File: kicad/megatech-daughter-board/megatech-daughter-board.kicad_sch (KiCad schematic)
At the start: 2 parts, among them J1 Conn_02x20_Counter_Clockwise, U1 Z084000xP

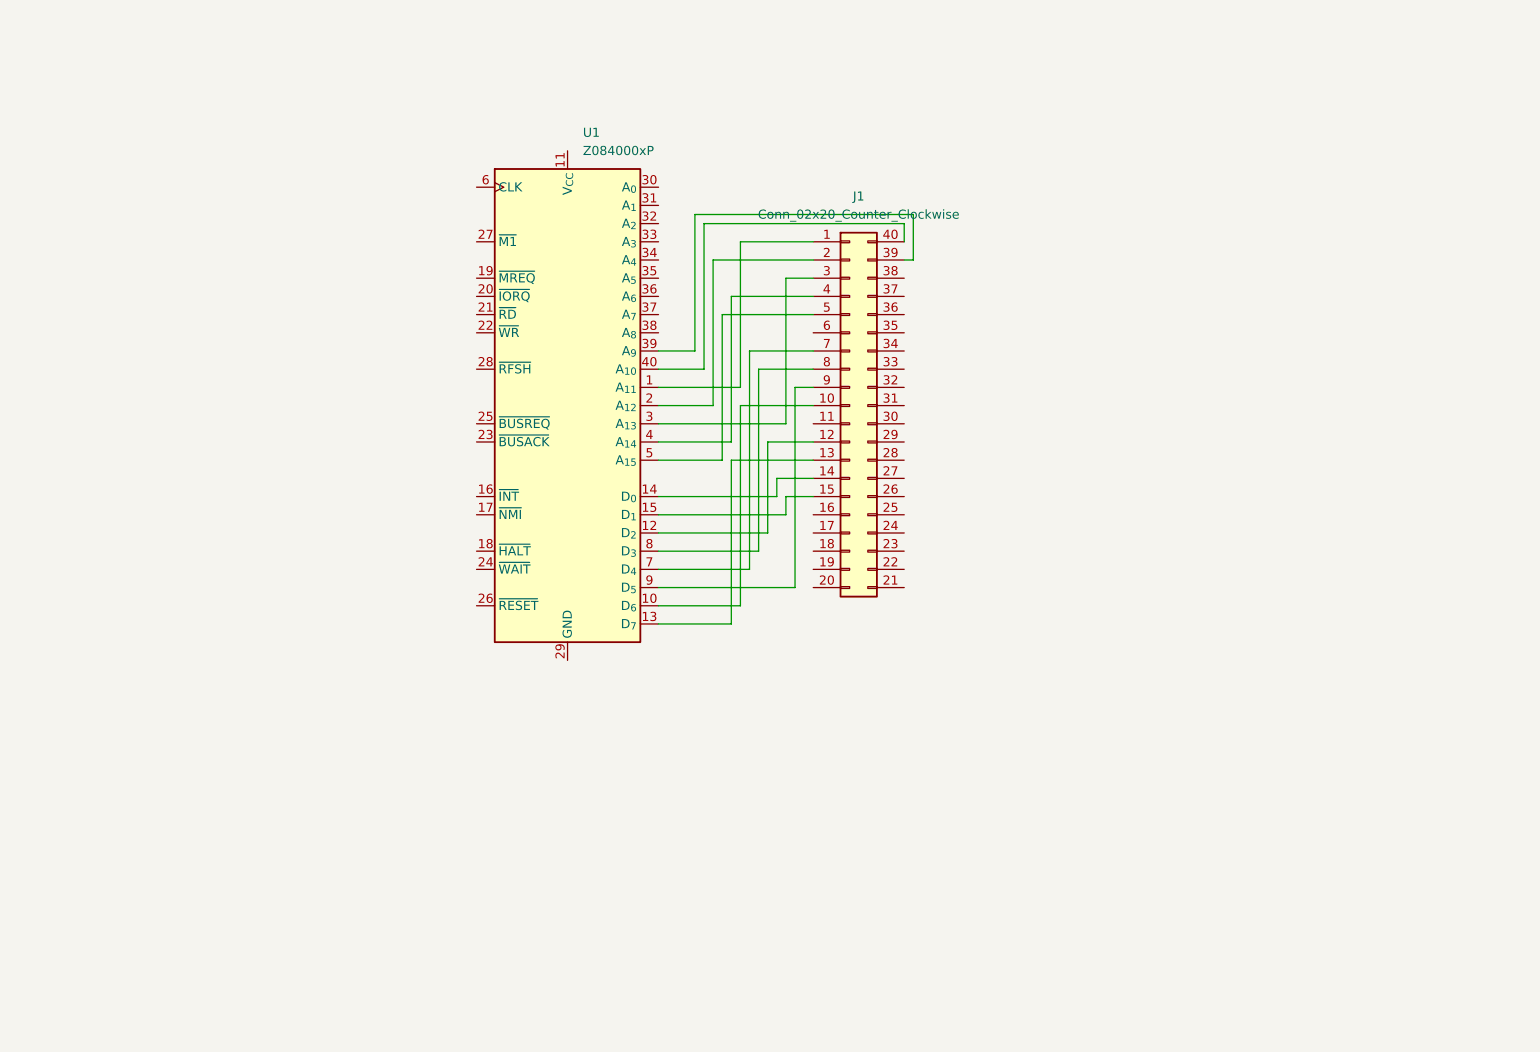
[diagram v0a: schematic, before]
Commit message: Placing more symbols
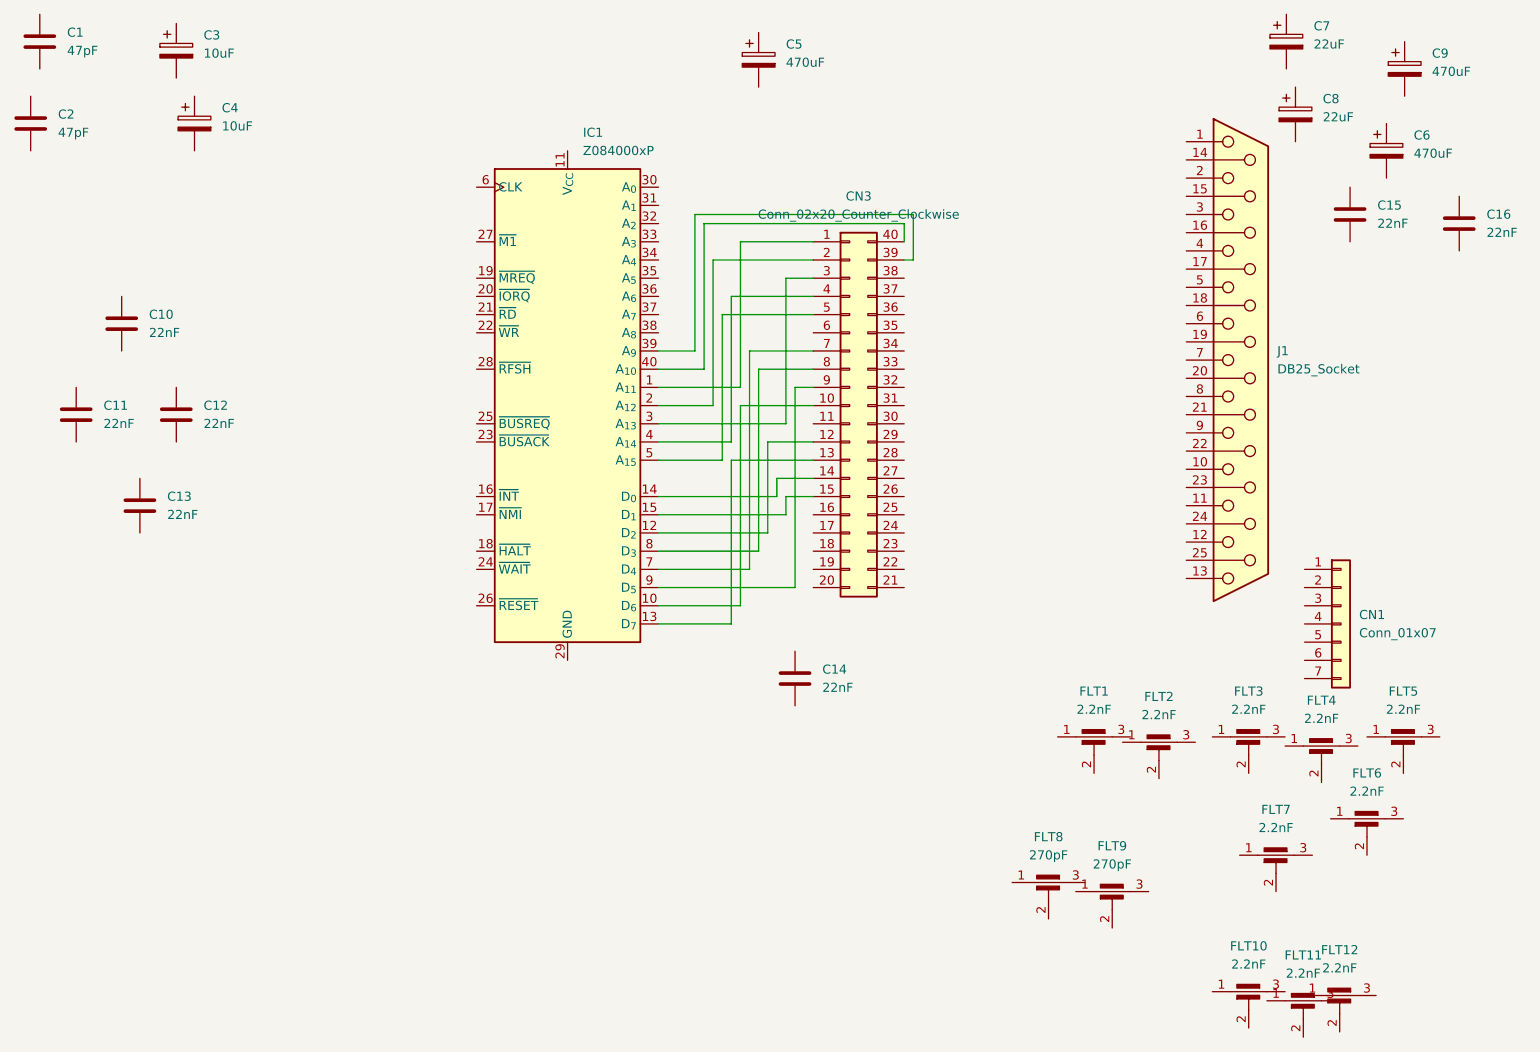
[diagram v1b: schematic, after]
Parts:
- added C1, C2: 47pF, Capacitor_THT:C_Disc_D4.3mm_W1.9mm_P5.00mm, symbol Device:C
- added C10, C11, C12, C13, C14, C15, C16: 22nF, Capacitor_THT:C_Disc_D6.0mm_W2.5mm_P5.00mm, symbol Device:C
- added C3, C4: 10uF, Capacitor_THT:C_Radial_D8.0mm_H11.5mm_P3.50mm, symbol Device:C_Polarized
- added C5, C6, C9: 470uF, Capacitor_THT:C_Radial_D10.0mm_H16.0mm_P5.00mm, symbol Device:C_Polarized
- added C7, C8: 22uF, Capacitor_THT:C_Radial_D8.0mm_H11.5mm_P3.50mm, symbol Device:C_Polarized
- added CN1: Conn_01x07, Connector_PinHeader_2.54mm:PinHeader_1x07_P2.54mm_Vertical, symbol Connector_Generic:Conn_01x07
- added FLT1, FLT10, FLT11, FLT12, FLT2, FLT3, FLT4, FLT5, FLT6, FLT7: 2.2nF, Filter:Filter_KEMET_PZB300_24.0x12.5mm_P10.0mm, symbol Device:Filter_EMI_C
- added FLT8, FLT9: 270pF, Filter:Filter_KEMET_PZB300_24.0x12.5mm_P10.0mm, symbol Device:Filter_EMI_C
- added J1: DB25_Socket, Connector_Dsub:DSUB-25_Socket_Vertical_P2.77x2.84mm, symbol Connector:DB25_Socket
- CN3: renamed from J1; footprint (none) -> Package_DIP:DIP-40_W15.24mm
- renumbered U1 to IC1

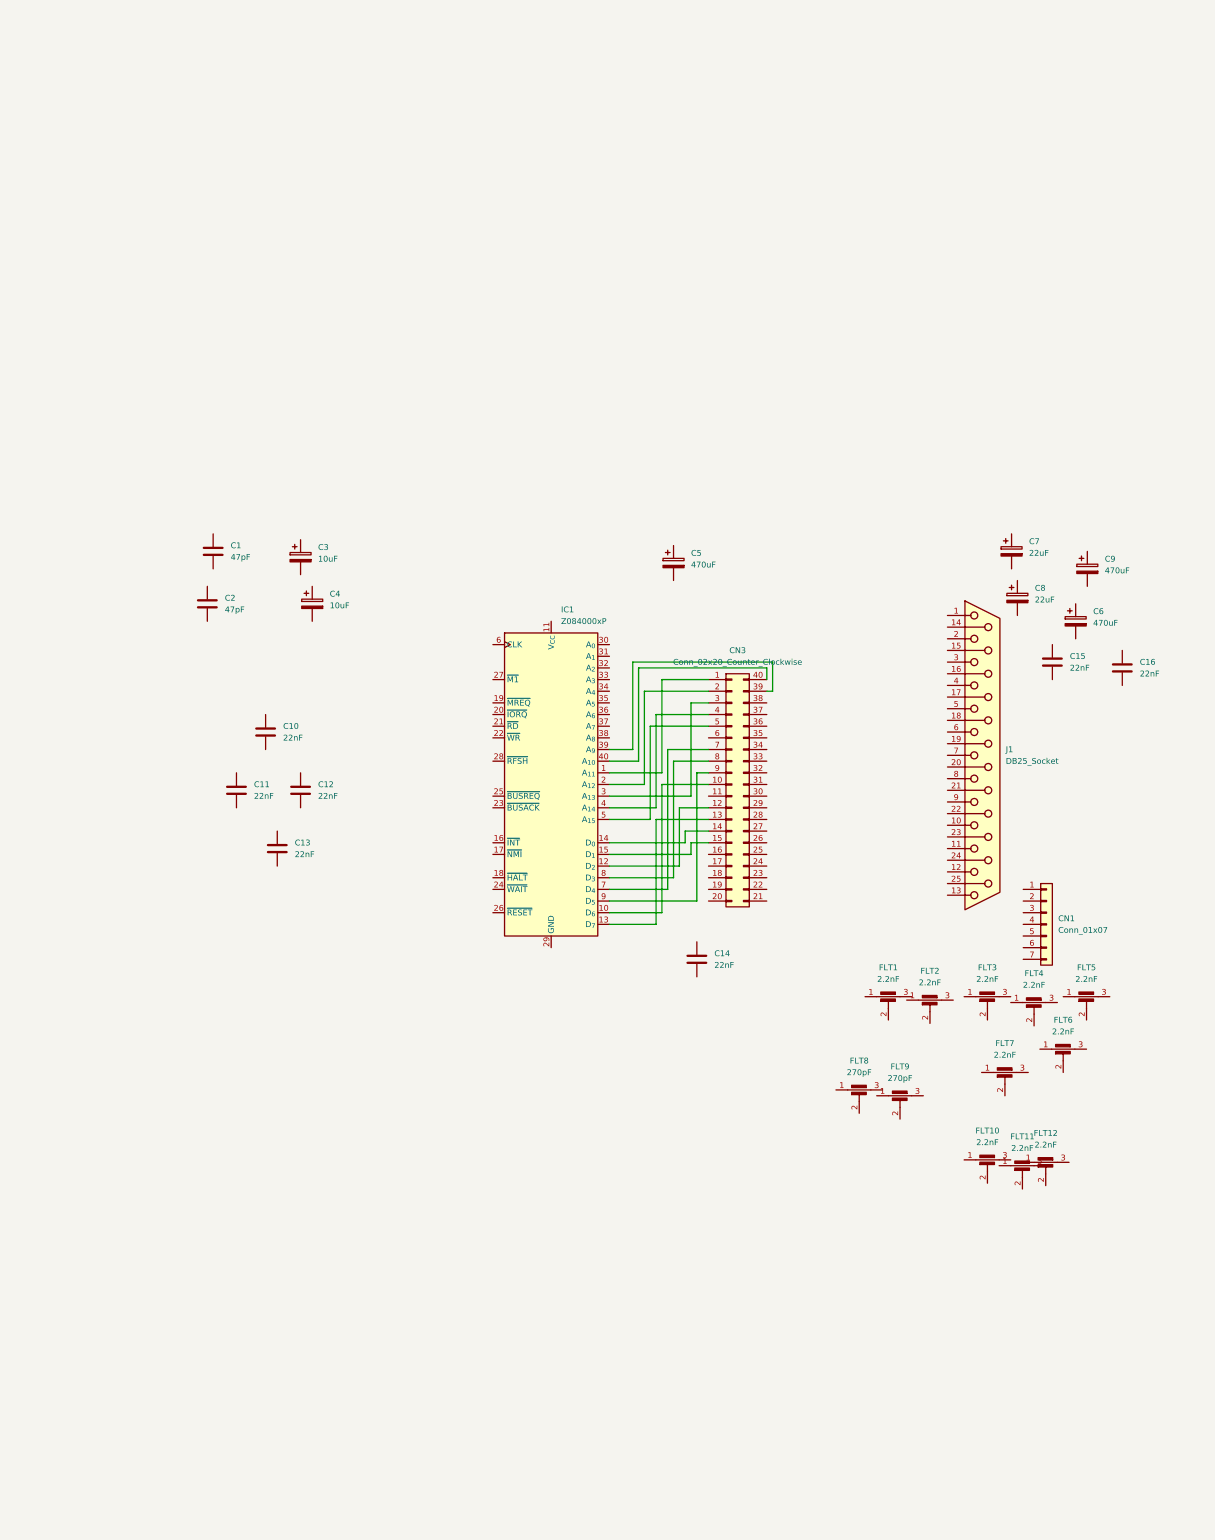
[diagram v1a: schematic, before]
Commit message: Further updates to daughter board pcb
All components now placed, but some connections still need to be made
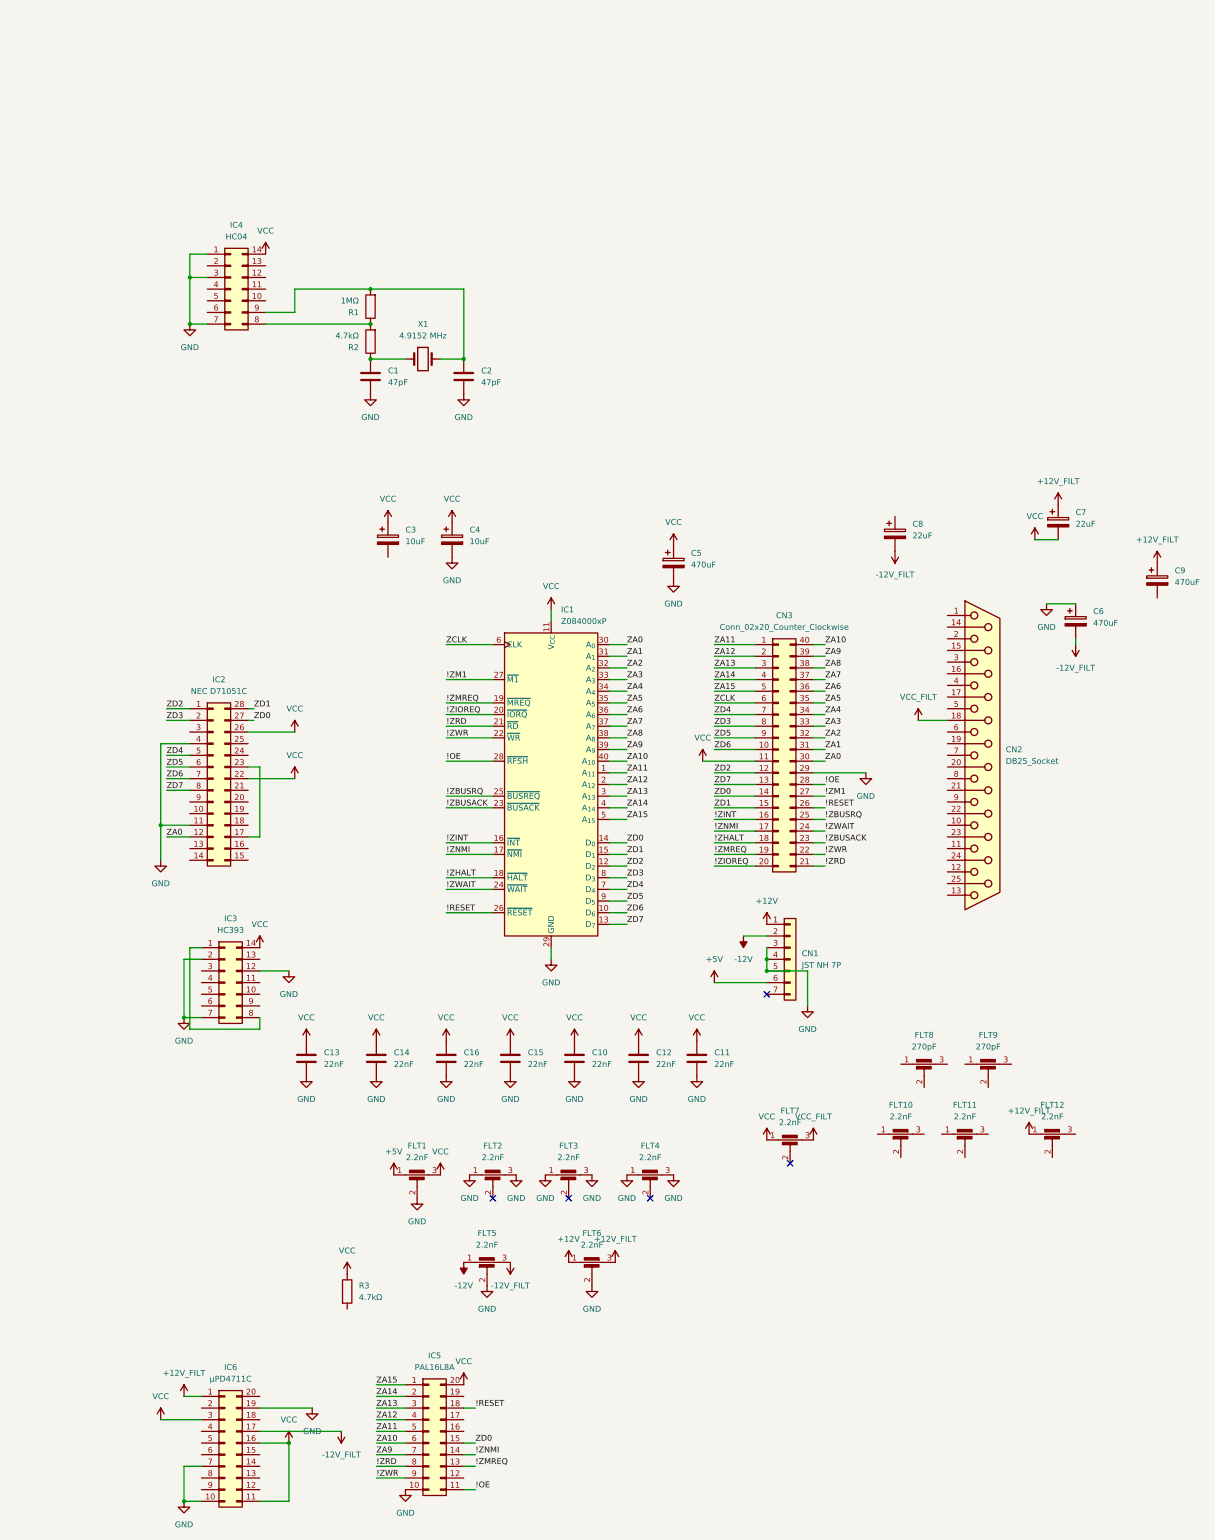
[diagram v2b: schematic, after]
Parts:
- added IC2: NEC D71051C, Package_DIP:DIP-28_W15.24mm, symbol Connector_Generic:Conn_02x14_Counter_Clockwise
- added IC3: HC393, Package_DIP:DIP-14_W7.62mm, symbol Connector_Generic:Conn_02x07_Counter_Clockwise
- added IC4: HC04, Package_DIP:DIP-14_W7.62mm, symbol Connector_Generic:Conn_02x07_Counter_Clockwise
- added IC5: PAL16L8A, Package_DIP:DIP-20_W7.62mm, symbol Connector_Generic:Conn_02x10_Counter_Clockwise
- added IC6: µPD4711C, Package_DIP:DIP-20_W7.62mm, symbol Connector_Generic:Conn_02x10_Counter_Clockwise
- added R1: 1MΩ, Resistor_THT:R_Axial_DIN0204_L3.6mm_D1.6mm_P5.08mm_Horizontal, symbol Device:R
- added R2, R3: 4.7kΩ, Resistor_THT:R_Axial_DIN0204_L3.6mm_D1.6mm_P5.08mm_Horizontal, symbol Device:R
- added X1: 4.9152 MHz, Crystal:Crystal_HC18-U_Horizontal, symbol Device:Crystal
- C3, C4, C7, C8: footprint Capacitor_THT:C_Radial_D8.0mm_H11.5mm_P3.50mm -> Capacitor_THT:CP_Radial_D5.0mm_P2.50mm
- C5, C6, C9: footprint Capacitor_THT:C_Radial_D10.0mm_H16.0mm_P5.00mm -> Capacitor_THT:CP_Radial_D10.0mm_P5.00mm
- CN1: value Conn_01x07 -> JST NH 7P
- FLT1, FLT10, FLT11, FLT12, FLT2, FLT3, FLT4, FLT5, FLT6, FLT7, FLT8, FLT9: footprint Filter:Filter_KEMET_PZB300_24.0x12.5mm_P10.0mm -> Crystal:Resonator-3Pin_W6.0mm_H3.0mm
- renumbered J1 to CN2
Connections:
- net GND: now reaches FLT3.1
- net GND: now also C1.2, C10.2, C11.2, C12.2, C13.2, C14.2, C15.2, C16.2, C2.2, C4.2, C5.2, C6.1, CN1.3 (Pin_3), CN1.4 (Pin_4), CN1.5 (Pin_5), CN3.29 (Pin_29), FLT1.2, FLT2.1, FLT2.3, FLT3.3, FLT4.1, FLT4.3, FLT5.2, FLT6.2, IC1.29 (GND), IC2.11 (Pin_11), IC2.4 (Pin_4), IC3.12 (Pin_12), IC3.2 (Pin_2), IC3.7 (Pin_7), IC4.1 (Pin_1), IC4.3 (Pin_3), IC4.7 (Pin_7), IC5.10 (Pin_10), IC6.10 (Pin_10), IC6.19 (Pin_19), IC6.7 (Pin_7)
- net -12V: now reaches FLT5.1
- net -12V: now also CN1.2 (Pin_2)
- net -12V_FILT: now reaches FLT5.3
- net -12V_FILT: now also C6.2, C8.2, IC6.17 (Pin_17)
- net +12V_FILT: now reaches C7.1
- net +12V_FILT: now also C9.1, FLT12.1, FLT6.3, IC6.1 (Pin_1)
- net VCC: now reaches C7.2
- net VCC: now also C10.1, C11.1, C12.1, C13.1, C14.1, C15.1, C16.1, C3.1, C4.1, C5.1, CN3.11 (Pin_11), FLT1.3, FLT7.1, IC1.11 (V_{CC}), IC2.22 (Pin_22), IC2.26 (Pin_26), IC3.14 (Pin_14), IC4.14 (Pin_14), IC5.20 (Pin_20), IC6.11 (Pin_11), IC6.16 (Pin_16), IC6.3 (Pin_3), R3.1
- net VCC_FILT: now reaches CN2.18 (P18)
- net VCC_FILT: now also FLT7.3
- net +12V: now reaches FLT6.1
- net +12V: now also CN1.1 (Pin_1)
- net at C1.1: now also R2.1, X1.1
- net at C2.1: now also IC4.9 (Pin_9), R1.2, X1.2
- net +5V: now reaches CN1.6 (Pin_6)
- net +5V: now also FLT1.1
- net ZA11: now reaches CN3.1 (Pin_1), IC1.1 (A_{11})
- net ZA11: now also IC5.5 (Pin_5)
- net ZD6: now reaches CN3.10 (Pin_10), IC1.10 (D_{6})
- net ZD6: now also IC2.7 (Pin_7)
- net ZD2: now reaches CN3.12 (Pin_12), IC1.12 (D_{2})
- net ZD2: now also IC2.1 (Pin_1)
- net ZD7: now reaches CN3.13 (Pin_13), IC1.13 (D_{7})
- net ZD7: now also IC2.8 (Pin_8)
- net ZD0: now reaches CN3.14 (Pin_14), IC1.14 (D_{0})
- net ZD0: now also IC2.27 (Pin_27), IC5.15 (Pin_15)
- net ZD1: now reaches CN3.15 (Pin_15), IC1.15 (D_{1})
- net ZD1: now also IC2.28 (Pin_28)
- net !ZINT: now reaches CN3.16 (Pin_16)
- net !ZINT: now also IC1.16 (~{INT})
- net !ZNMI: now reaches CN3.17 (Pin_17)
- net !ZNMI: now also IC1.17 (~{NMI}), IC5.14 (Pin_14)
- net !ZHALT: now reaches CN3.18 (Pin_18)
- net !ZHALT: now also IC1.18 (~{HALT})
- net !ZMREQ: now reaches CN3.19 (Pin_19)
- net !ZMREQ: now also IC1.19 (~{MREQ}), IC5.13 (Pin_13)
- net ZA12: now reaches CN3.2 (Pin_2), IC1.2 (A_{12})
- net ZA12: now also IC5.4 (Pin_4)
- net !ZIOREQ: now reaches CN3.20 (Pin_20)
- net !ZIOREQ: now also IC1.20 (~{IORQ})
- net !ZRD: now reaches CN3.21 (Pin_21)
- net !ZRD: now also IC1.21 (~{RD}), IC5.8 (Pin_8)
- net !ZWR: now reaches CN3.22 (Pin_22)
- net !ZWR: now also IC1.22 (~{WR}), IC5.9 (Pin_9)
- net !ZBUSACK: now reaches CN3.23 (Pin_23)
- net !ZBUSACK: now also IC1.23 (~{BUSACK})
- net !ZWAIT: now reaches CN3.24 (Pin_24)
- net !ZWAIT: now also IC1.24 (~{WAIT})
- net !ZBUSRQ: now reaches CN3.25 (Pin_25)
- net !ZBUSRQ: now also IC1.25 (~{BUSREQ})
- net !RESET: now reaches CN3.26 (Pin_26)
- net !RESET: now also IC1.26 (~{RESET}), IC5.18 (Pin_18)
- net !ZM1: now reaches CN3.27 (Pin_27)
- net !ZM1: now also IC1.27 (~{M1})
- net !OE: now reaches CN3.28 (Pin_28)
- net !OE: now also IC1.28 (~{RFSH}), IC5.11 (Pin_11)
- net ZA13: now reaches CN3.3 (Pin_3), IC1.3 (A_{13})
- net ZA13: now also IC5.3 (Pin_3)
- net ZA0: now reaches CN3.30 (Pin_30)
- net ZA0: now also IC1.30 (A_{0}), IC2.12 (Pin_12)
- net ZA1: now reaches CN3.31 (Pin_31)
- net ZA1: now also IC1.31 (A_{1})
- net ZA2: now reaches CN3.32 (Pin_32)
- net ZA2: now also IC1.32 (A_{2})
- net ZA3: now reaches CN3.33 (Pin_33)
- net ZA3: now also IC1.33 (A_{3})
- net ZA4: now reaches CN3.34 (Pin_34)
- net ZA4: now also IC1.34 (A_{4})
- net ZA5: now reaches CN3.35 (Pin_35)
- net ZA5: now also IC1.35 (A_{5})
- net ZA6: now reaches CN3.36 (Pin_36)
- net ZA6: now also IC1.36 (A_{6})
- net ZA7: now reaches CN3.37 (Pin_37)
- net ZA7: now also IC1.37 (A_{7})
- net ZA8: now reaches CN3.38 (Pin_38)
- net ZA8: now also IC1.38 (A_{8})
- net ZA9: now reaches CN3.39 (Pin_39), IC1.39 (A_{9})
- net ZA9: now also IC5.7 (Pin_7)
- net ZA14: now reaches CN3.4 (Pin_4), IC1.4 (A_{14})
- net ZA14: now also IC5.2 (Pin_2)
- net ZA10: now reaches CN3.40 (Pin_40), IC1.40 (A_{10})
- net ZA10: now also IC5.6 (Pin_6)
- net ZA15: now reaches CN3.5 (Pin_5), IC1.5 (A_{15})
- net ZA15: now also IC5.1 (Pin_1)
- net ZCLK: now reaches CN3.6 (Pin_6)
- net ZCLK: now also IC1.6 (CLK)
- net ZD4: now reaches CN3.7 (Pin_7), IC1.7 (D_{4})
- net ZD4: now also IC2.5 (Pin_5)
- net ZD3: now reaches CN3.8 (Pin_8), IC1.8 (D_{3})
- net ZD3: now also IC2.2 (Pin_2)
- net ZD5: now reaches CN3.9 (Pin_9), IC1.9 (D_{5})
- net ZD5: now also IC2.6 (Pin_6)
- new net: IC4.8 (Pin_8), R1.1, R2.2
- new net: IC3.1 (Pin_1), IC3.8 (Pin_8)
- new net: IC2.17 (Pin_17), IC2.23 (Pin_23)
- no-connect marks 0 -> 5
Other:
- moved on the sheet: C1, C10, C11, C12, C13, C14, C15, C16, C2, C3, C4, C7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
